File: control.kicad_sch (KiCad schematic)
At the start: 0 parts

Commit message: Design power
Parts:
- added BT_EN, STORAGE_EN, TRANSLATION_EN: SLW-864587-2A-RA-N-D, SLW-864587-2A-RA-N-D:SW_SLW-864587-2A-RA-N-D, symbol SLW-864587-2A-RA-N-D:SLW-864587-2A-RA-N-D
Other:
- title: Port Plover -> Stenoswitch

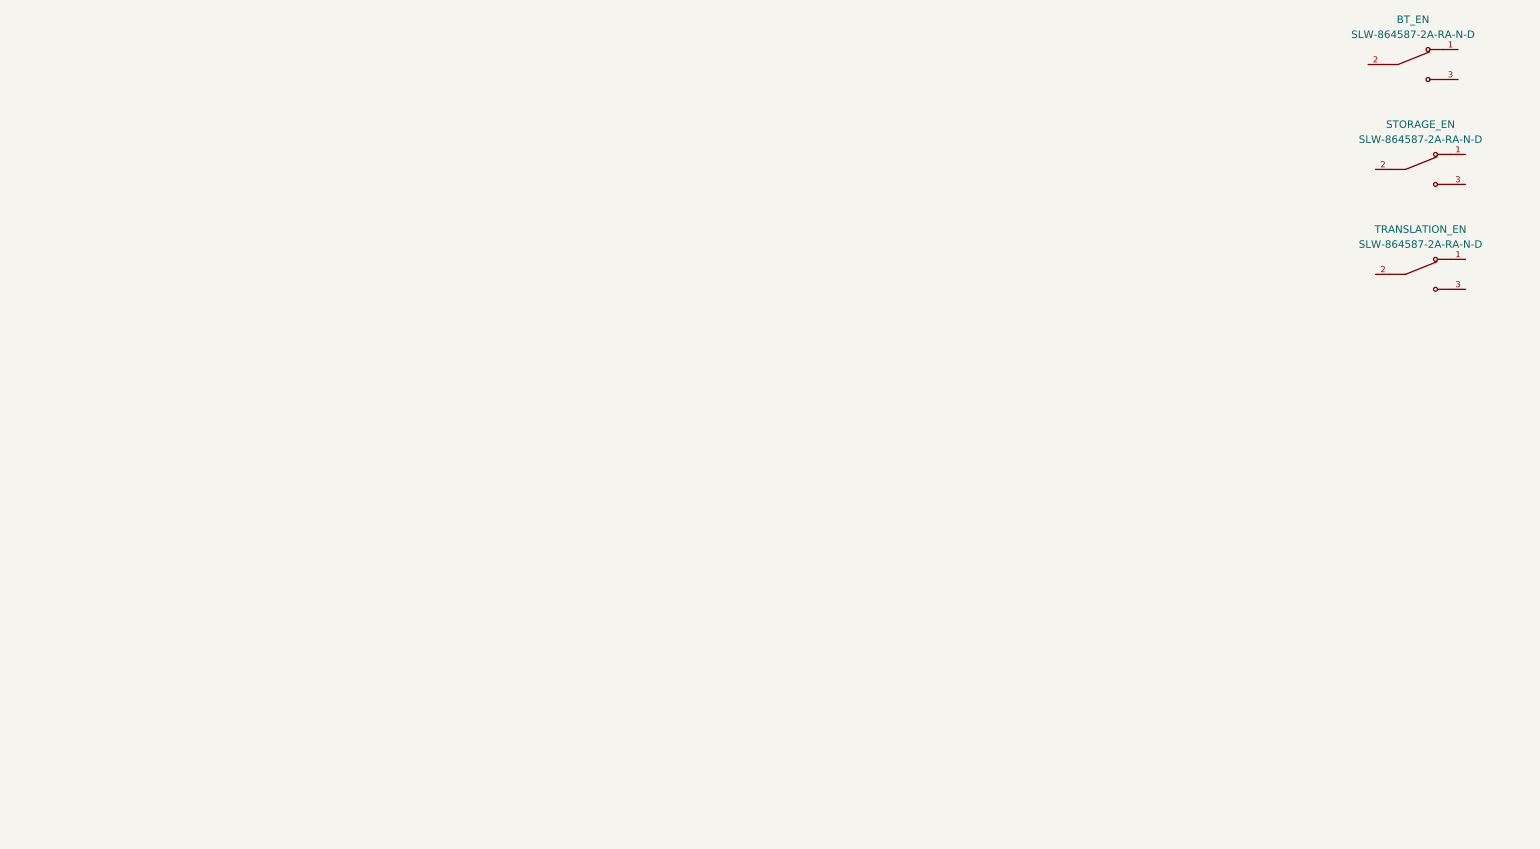
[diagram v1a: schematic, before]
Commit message: Rework battery entirely
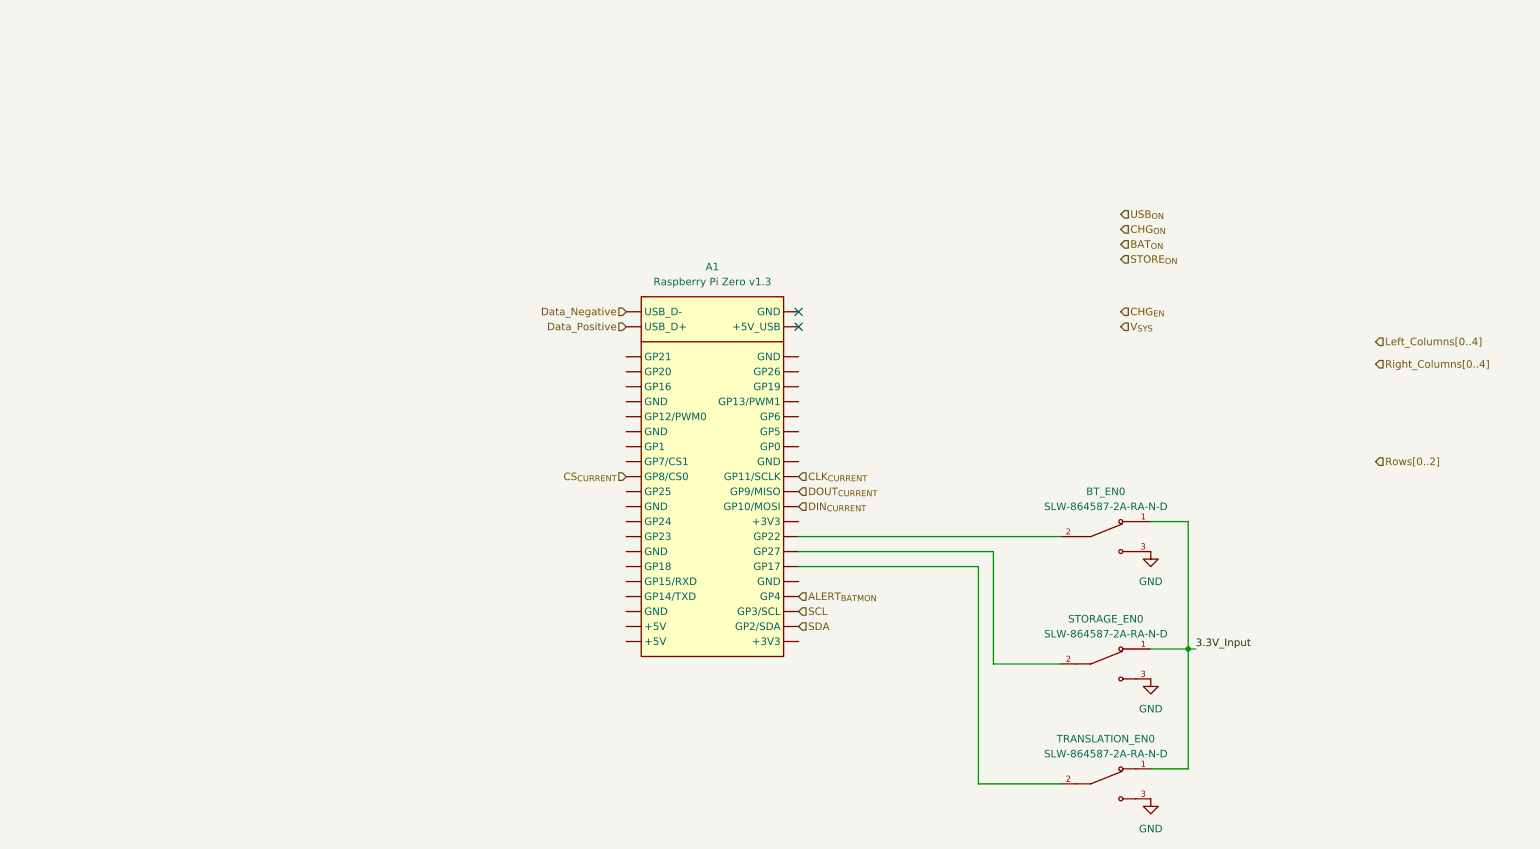
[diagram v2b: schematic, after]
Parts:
- added A1: Raspberry Pi Zero v1.3, Raspberry_Pi_Zero_v.1.3_Hat:RASPI_ZERO_FULL, symbol Raspberry_Pi_Zero_v.1.3_Hat:Raspberry_Pi_Zero_v.1.3_Hat
- renumbered BT_EN to BT_EN0, STORAGE_EN to STORAGE_EN0, TRANSLATION_EN to TRANSLATION_EN0
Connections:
- net 3.3V_Input: now reaches TRANSLATION_EN0.1
- net 3.3V_Input: now also BT_EN0.1, STORAGE_EN0.1
- net at TRANSLATION_EN0.2: now also A1.11 (GP17)
- net GND: now reaches TRANSLATION_EN0.3
- net GND: now also BT_EN0.3, STORAGE_EN0.3
- net at STORAGE_EN0.2: now also A1.13 (GP27)
- net at BT_EN0.2: now also A1.15 (GP22)
- new net ALERT_{BATMON}: A1.7 (GP4)
- new net CLK_{CURRENT}: A1.23 (GP11/SCLK)
- new net CS_{CURRENT}: A1.24 (GP8/CS0)
- new net DIN_{CURRENT}: A1.19 (GP10/MOSI)
- new net DOUT_{CURRENT}: A1.21 (GP9/MISO)
- new net Data_Negative: A1.PP23 (USB_D-)
- new net Data_Positive: A1.PP22 (USB_D+)
- new net SCL: A1.5 (GP3/SCL)
- new net SDA: A1.3 (GP2/SDA)
- no-connect marks 0 -> 2
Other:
- moved on the sheet: BT_EN0, STORAGE_EN0, TRANSLATION_EN0

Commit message: Assign footprints
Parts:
- BT_EN0, STORAGE_EN0, TRANSLATION_EN0: footprint SLW-864587-2A-RA-N-D:SW_SLW-864587-2A-RA-N-D -> SW_SLW-864587-2A-RA-N-D
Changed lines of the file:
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@@
 			)
 		)
-		(property "Footprint" "SLW-864587-2A-RA-N-D:SW_SLW-864587-2A-RA-N-D"
+		(property "Footprint" "SW_SLW-864587-2A-RA-N-D"
 			(at 208.28 148.59 0)
 			(effects
@@
 			)
 		)
-		(property "Footprint" "SLW-864587-2A-RA-N-D:SW_SLW-864587-2A-RA-N-D"
+		(property "Footprint" "SW_SLW-864587-2A-RA-N-D"
 			(at 208.28 128.27 0)
 			(effects
@@
 			)
 		)
-		(property "Footprint" "SLW-864587-2A-RA-N-D:SW_SLW-864587-2A-RA-N-D"
+		(property "Footprint" "SW_SLW-864587-2A-RA-N-D"
 			(at 208.28 106.68 0)
 			(effects

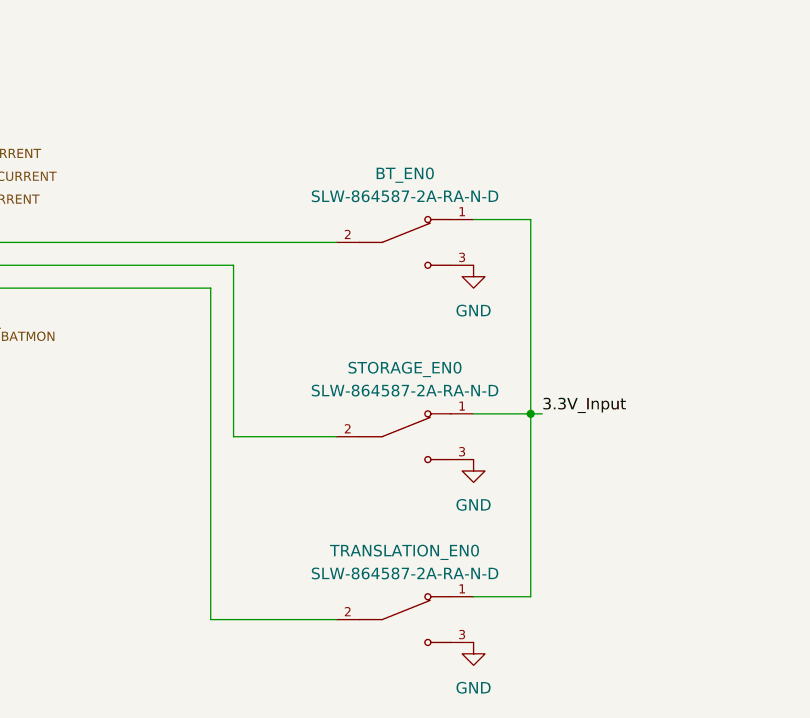
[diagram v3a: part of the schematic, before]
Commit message: Init right and left PCBs
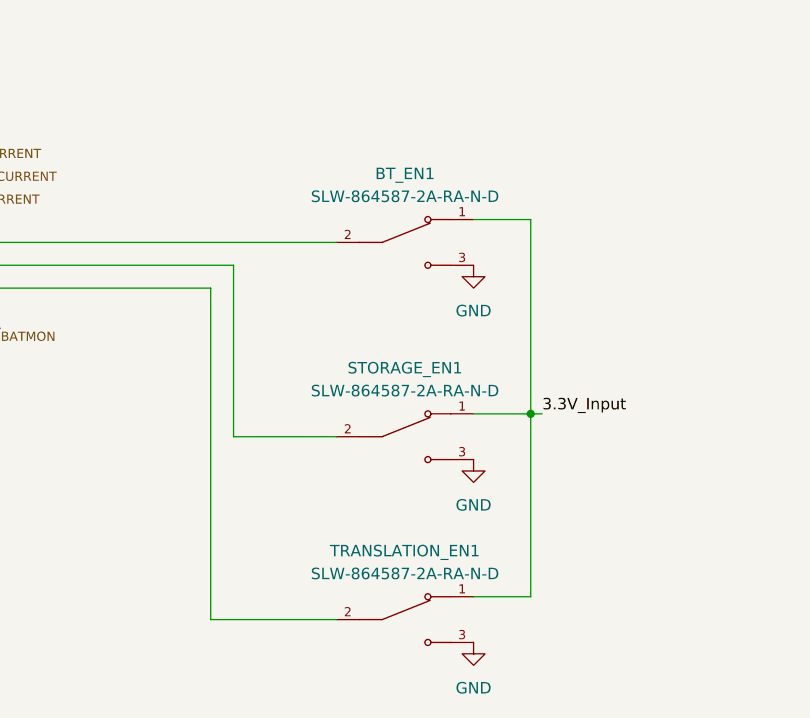
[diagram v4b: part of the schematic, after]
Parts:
- renumbered BT_EN0 to BT_EN1, STORAGE_EN0 to STORAGE_EN1, TRANSLATION_EN0 to TRANSLATION_EN1
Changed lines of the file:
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@@
 		(dnp no)
 		(fields_autoplaced yes)
-		(property "Reference" "TRANSLATION_EN0"
+		(property "Reference" "TRANSLATION_EN1"
 			(at 208.28 140.97 0)
 			(effects
@@
 				(path "/06a6eca0-edda-4cc0-a23f-017602e67f07/99f3b279-b2b0-4dd5-ab05-9b518546ce95/93dd658d-093b-457b-aa9d-06e2289958ef"
 					(reference "TRANSLATION_EN0")
+					(unit 1)
+				)
+			)
+			(project "right_hand"
+				(path "/efcccfe8-5e20-4b1b-8d3b-61fce771481e/93dd658d-093b-457b-aa9d-06e2289958ef"
+					(reference "TRANSLATION_EN1")
 					(unit 1)
 				)
@@
 		(dnp no)
 		(fields_autoplaced yes)
-		(property "Reference" "STORAGE_EN0"
+		(property "Reference" "STORAGE_EN1"
 			(at 208.28 120.65 0)
 			(effects
@@
 				(path "/06a6eca0-edda-4cc0-a23f-017602e67f07/99f3b279-b2b0-4dd5-ab05-9b518546ce95/93dd658d-093b-457b-aa9d-06e2289958ef"
 					(reference "STORAGE_EN0")
+					(unit 1)
+				)
+			)
+			(project "right_hand"
+				(path "/efcccfe8-5e20-4b1b-8d3b-61fce771481e/93dd658d-093b-457b-aa9d-06e2289958ef"
+					(reference "STORAGE_EN1")
 					(unit 1)
 				)
@@
 		(dnp no)
 		(fields_autoplaced yes)
-		(property "Reference" "#PWR014"
+		(property "Reference" "#PWR0127"
 			(at 215.9 137.16 0)
 			(effects
@@
 				(path "/06a6eca0-edda-4cc0-a23f-017602e67f07/99f3b279-b2b0-4dd5-ab05-9b518546ce95/93dd658d-093b-457b-aa9d-06e2289958ef"
 					(reference "#PWR014")
+					(unit 1)
+				)
+			)
+			(project "right_hand"
+				(path "/efcccfe8-5e20-4b1b-8d3b-61fce771481e/93dd658d-093b-457b-aa9d-06e2289958ef"
+					(reference "#PWR0127")
 					(unit 1)
 				)
@@
 		(dnp no)
 		(fields_autoplaced yes)
-		(property "Reference" "BT_EN0"
+		(property "Reference" "BT_EN1"
 			(at 208.28 99.06 0)
 			(effects
@@
 				(path "/06a6eca0-edda-4cc0-a23f-017602e67f07/99f3b279-b2b0-4dd5-ab05-9b518546ce95/93dd658d-093b-457b-aa9d-06e2289958ef"
 					(reference "BT_EN0")
+					(unit 1)
+				)
+			)
+			(project "right_hand"
+				(path "/efcccfe8-5e20-4b1b-8d3b-61fce771481e/93dd658d-093b-457b-aa9d-06e2289958ef"
+					(reference "BT_EN1")
 					(unit 1)
 				)
@@
 				)
 			)
+			(project "right_hand"
+				(path "/efcccfe8-5e20-4b1b-8d3b-61fce771481e/93dd658d-093b-457b-aa9d-06e2289958ef"
+					(reference "A1")
+					(unit 1)
+				)
+			)
 		)
 	)
@@
 		(dnp no)
 		(fields_autoplaced yes)
-		(property "Reference" "#PWR00"
+		(property "Reference" "#PWR0128"
 			(at 215.9 115.57 0)
 			(effects
@@
 				(path "/06a6eca0-edda-4cc0-a23f-017602e67f07/99f3b279-b2b0-4dd5-ab05-9b518546ce95/93dd658d-093b-457b-aa9d-06e2289958ef"
 					(reference "#PWR00")
+					(unit 1)
+				)
+			)
+			(project "right_hand"
+				(path "/efcccfe8-5e20-4b1b-8d3b-61fce771481e/93dd658d-093b-457b-aa9d-06e2289958ef"
+					(reference "#PWR0128")
 					(unit 1)
 				)
@@
 		(dnp no)
 		(fields_autoplaced yes)
-		(property "Reference" "#PWR015"
+		(property "Reference" "#PWR0126"
 			(at 215.9 157.48 0)
 			(effects
@@
 					(unit 1)
 				)
+			)
+			(project "right_hand"
+				(path "/efcccfe8-5e20-4b1b-8d3b-61fce771481e/93dd658d-093b-457b-aa9d-06e2289958ef"
+					(reference "#PWR0126")
+					(unit 1)
+				)

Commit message: Rename keyswitch diodes
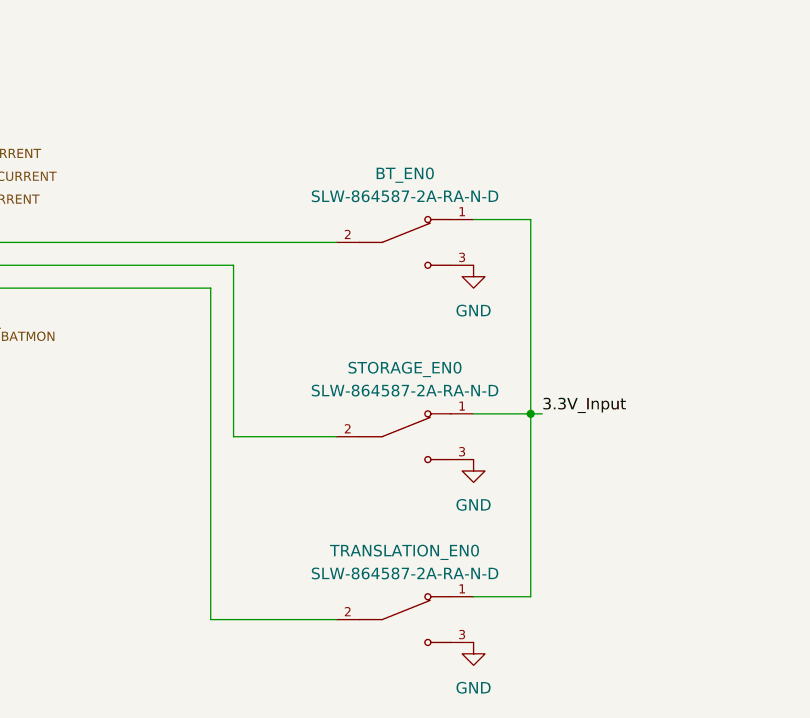
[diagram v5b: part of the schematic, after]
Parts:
- renumbered BT_EN1 to BT_EN0, STORAGE_EN1 to STORAGE_EN0, TRANSLATION_EN1 to TRANSLATION_EN0
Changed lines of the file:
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@@
 		(dnp no)
 		(fields_autoplaced yes)
-		(property "Reference" "TRANSLATION_EN1"
+		(property "Reference" "TRANSLATION_EN0"
 			(at 208.28 140.97 0)
 			(effects
@@
 		(dnp no)
 		(fields_autoplaced yes)
-		(property "Reference" "STORAGE_EN1"
+		(property "Reference" "STORAGE_EN0"
 			(at 208.28 120.65 0)
 			(effects
@@
 		(dnp no)
 		(fields_autoplaced yes)
-		(property "Reference" "#PWR0127"
+		(property "Reference" "#PWR014"
 			(at 215.9 137.16 0)
 			(effects
@@
 		(dnp no)
 		(fields_autoplaced yes)
-		(property "Reference" "BT_EN1"
+		(property "Reference" "BT_EN0"
 			(at 208.28 99.06 0)
 			(effects
@@
 		(dnp no)
 		(fields_autoplaced yes)
-		(property "Reference" "#PWR0128"
+		(property "Reference" "#PWR00"
 			(at 215.9 115.57 0)
 			(effects
@@
 		(dnp no)
 		(fields_autoplaced yes)
-		(property "Reference" "#PWR0126"
+		(property "Reference" "#PWR015"
 			(at 215.9 157.48 0)
 			(effects

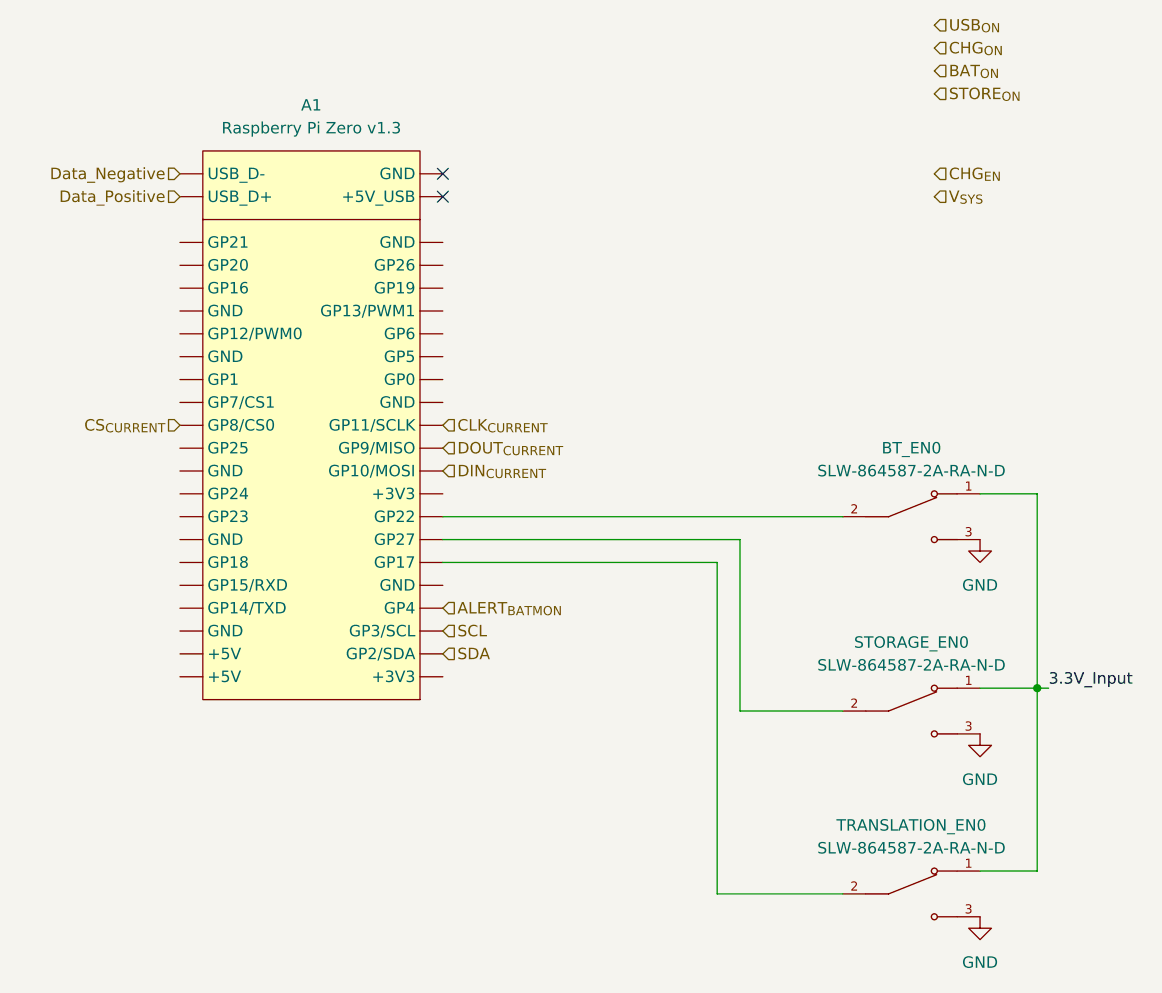
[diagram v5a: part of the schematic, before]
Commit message: Complete most of RHS layout
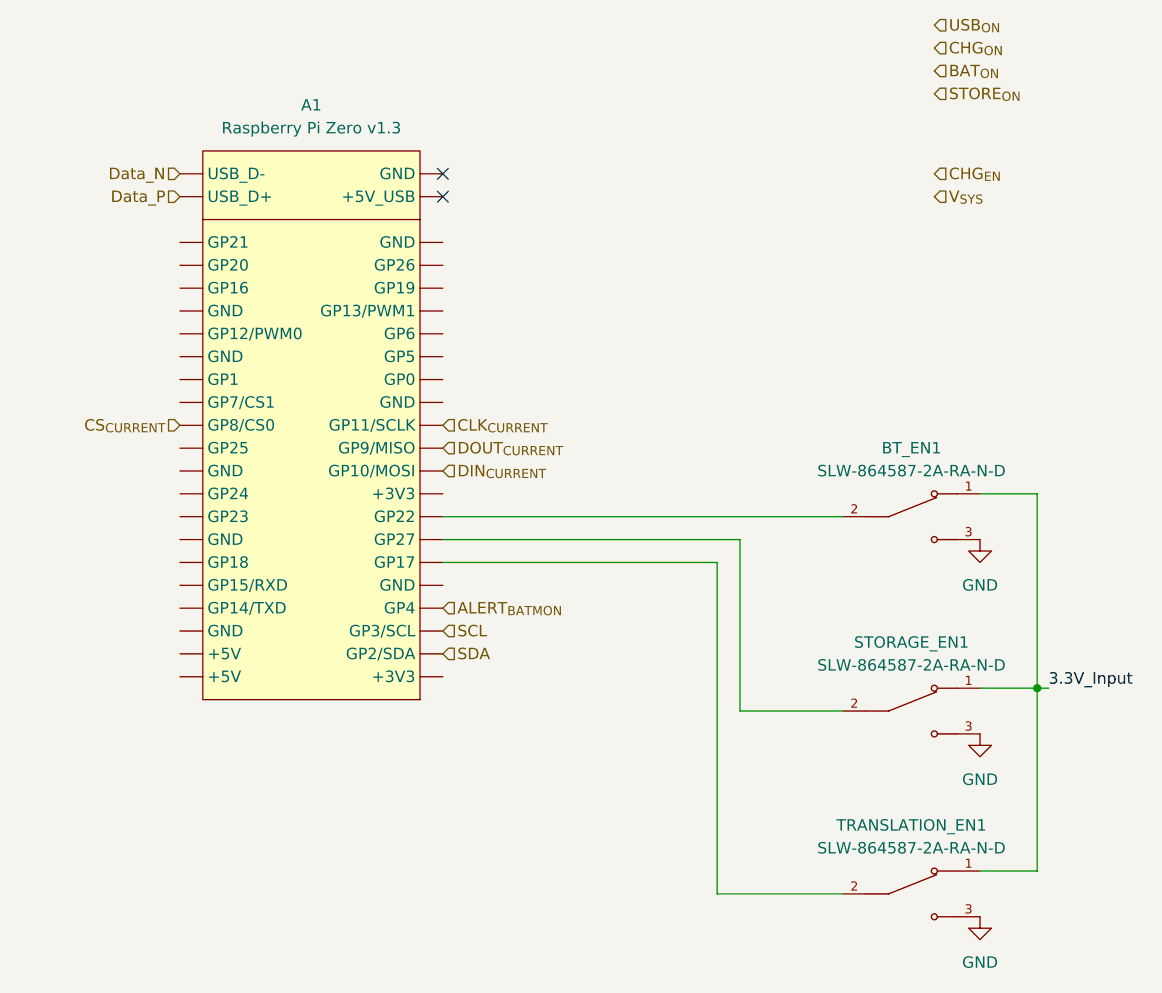
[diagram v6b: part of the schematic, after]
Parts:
- renumbered BT_EN0 to BT_EN1, STORAGE_EN0 to STORAGE_EN1, TRANSLATION_EN0 to TRANSLATION_EN1
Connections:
- net Data_Negative renamed Data_N
- net Data_Positive renamed Data_P
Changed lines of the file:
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@@
 		)
 	)
-	(hierarchical_label "Data_Negative"
+	(hierarchical_label "Data_N"
 		(shape input)
 		(at 127 68.58 180)
@@
 		)
 	)
-	(hierarchical_label "Data_Positive"
+	(hierarchical_label "Data_P"
 		(shape input)
 		(at 127 71.12 180)
@@
 		(dnp no)
 		(fields_autoplaced yes)
-		(property "Reference" "TRANSLATION_EN0"
+		(property "Reference" "TRANSLATION_EN1"
 			(at 208.28 140.97 0)
 			(effects
@@
 		(dnp no)
 		(fields_autoplaced yes)
-		(property "Reference" "STORAGE_EN0"
+		(property "Reference" "STORAGE_EN1"
 			(at 208.28 120.65 0)
 			(effects
@@
 		(dnp no)
 		(fields_autoplaced yes)
-		(property "Reference" "#PWR014"
+		(property "Reference" "#PWR0127"
 			(at 215.9 137.16 0)
 			(effects
@@
 		(dnp no)
 		(fields_autoplaced yes)
-		(property "Reference" "BT_EN0"
+		(property "Reference" "BT_EN1"
 			(at 208.28 99.06 0)
 			(effects
@@
 		(dnp no)
 		(fields_autoplaced yes)
-		(property "Reference" "#PWR00"
+		(property "Reference" "#PWR0128"
 			(at 215.9 115.57 0)
 			(effects
@@
 		(dnp no)
 		(fields_autoplaced yes)
-		(property "Reference" "#PWR015"
+		(property "Reference" "#PWR0126"
 			(at 215.9 157.48 0)
 			(effects

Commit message: Rework right hand
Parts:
- renumbered BT_EN1 to BT_EN0, STORAGE_EN1 to STORAGE_EN0, TRANSLATION_EN1 to TRANSLATION_EN0
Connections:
- net 3.3V_Input is gone; now on an unnamed net: BT_EN0.1, STORAGE_EN0.1, TRANSLATION_EN0.1
- net BAT_{ON}: now also A1.16 (GP23)
- net CHG_{EN}: now also A1.10 (GP15/RXD)
- net CHG_{ON}: now also A1.18 (GP24)
- net GND: now also A1.14 (GND), A1.25 (GND), A1.30 (GND), A1.34 (GND), A1.9 (GND)
- net STORE_{ON}: now also A1.26 (GP7/CS1)
- net USB_{ON}: now also A1.12 (GP18)
- net V_{SYS}: now also A1.2 (+5V), A1.4 (+5V)
- net at TRANSLATION_EN0.2: now also A1.31 (GP6); no longer A1.11 (GP17)
- net at STORAGE_EN0.2: now also A1.29 (GP5); no longer A1.13 (GP27)
- net at BT_EN0.2: now also A1.27 (GP0); no longer A1.15 (GP22)
- net Left_Columns0: now reaches A1.28 (GP1)
- net Left_Columns1: now reaches A1.32 (GP12/PWM0)
- net Rows0: now reaches A1.33 (GP13/PWM1)
- net Right_Columns0: now reaches A1.35 (GP19)
- net Left_Columns2: now reaches A1.36 (GP16)
- net Right_Columns1: now reaches A1.37 (GP26)
- net Left_Columns3: now reaches A1.38 (GP20)
- net Left_Columns4: now reaches A1.40 (GP21)
- net Right_Columns3: now reaches A1.8 (GP14/TXD)
- new net Rows1: A1.15 (GP22)
- new net Rows2: A1.11 (GP17)
- no-connect marks 2 -> 8
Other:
- moved on the sheet: A1, BT_EN0, STORAGE_EN0, TRANSLATION_EN0
